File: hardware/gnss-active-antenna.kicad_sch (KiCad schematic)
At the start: 17 parts, among them J1 CONMCX002-SMD, U1 MAX2659ELT+T, U2 MIC5205-2.5YM5

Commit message: main: hardware: schematic update
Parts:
- C1: value 470pF -> 24pF
- C2: value 100 pF -> 24 pF
- C4: value 470 pF -> 33 nF
- C5: value 2.2 uF -> 10 uF
- C6: value 33 pF -> 33 nF
- L1: value 6.8 nH -> 6.2 nH
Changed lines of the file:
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@@
 			)
 		)
-		(property "Value" "6.8 nH"
+		(property "Value" "6.2 nH"
 			(at 99.06 48.26 90)
 			(effects
@@
 			)
 		)
-		(property "Value" "33 pF"
+		(property "Value" "33 nF"
 			(at 190.5 71.1199 0)
 			(effects
@@
 		(on_board yes)
 		(dnp no)
-		(fields_autoplaced yes)
 		(property "Reference" "C4"
-			(at 101.6 144.7799 0)
-			(effects
-				(font
-					(size 1.27 1.27)
-				)
-				(justify left)
-			)
-		)
-		(property "Value" "470 pF"
-			(at 101.6 147.3199 0)
-			(effects
-				(font
-					(size 1.27 1.27)
-				)
-				(justify left)
+			(at 101.854 148.844 0)
+			(effects
+				(font
+					(size 1.27 1.27)
+				)
+				(justify right)
+			)
+		)
+		(property "Value" "33 nF"
+			(at 107.442 149.352 0)
+			(effects
+				(font
+					(size 1.27 1.27)
+				)
+				(justify right)
 			)
 		)
@@
 			)
 		)
-		(property "Value" "100 pF"
+		(property "Value" "24 pF"
 			(at 229.87 49.53 90)
 			(effects
@@
 		(dnp no)
 		(property "Reference" "C5"
-			(at 113.03 144.7799 0)
+			(at 116.078 142.494 0)
 			(effects
 				(font
@@
 			)
 		)
-		(property "Value" "2.2 uF"
-			(at 113.03 147.3199 0)
+		(property "Value" "10 uF"
+			(at 125.222 143.51 0)
 			(effects
 				(font
@@
 			)
 		)
-		(property "Value" "470pF"
+		(property "Value" "24pF"
 			(at 86.36 45.72 90)
 			(effects

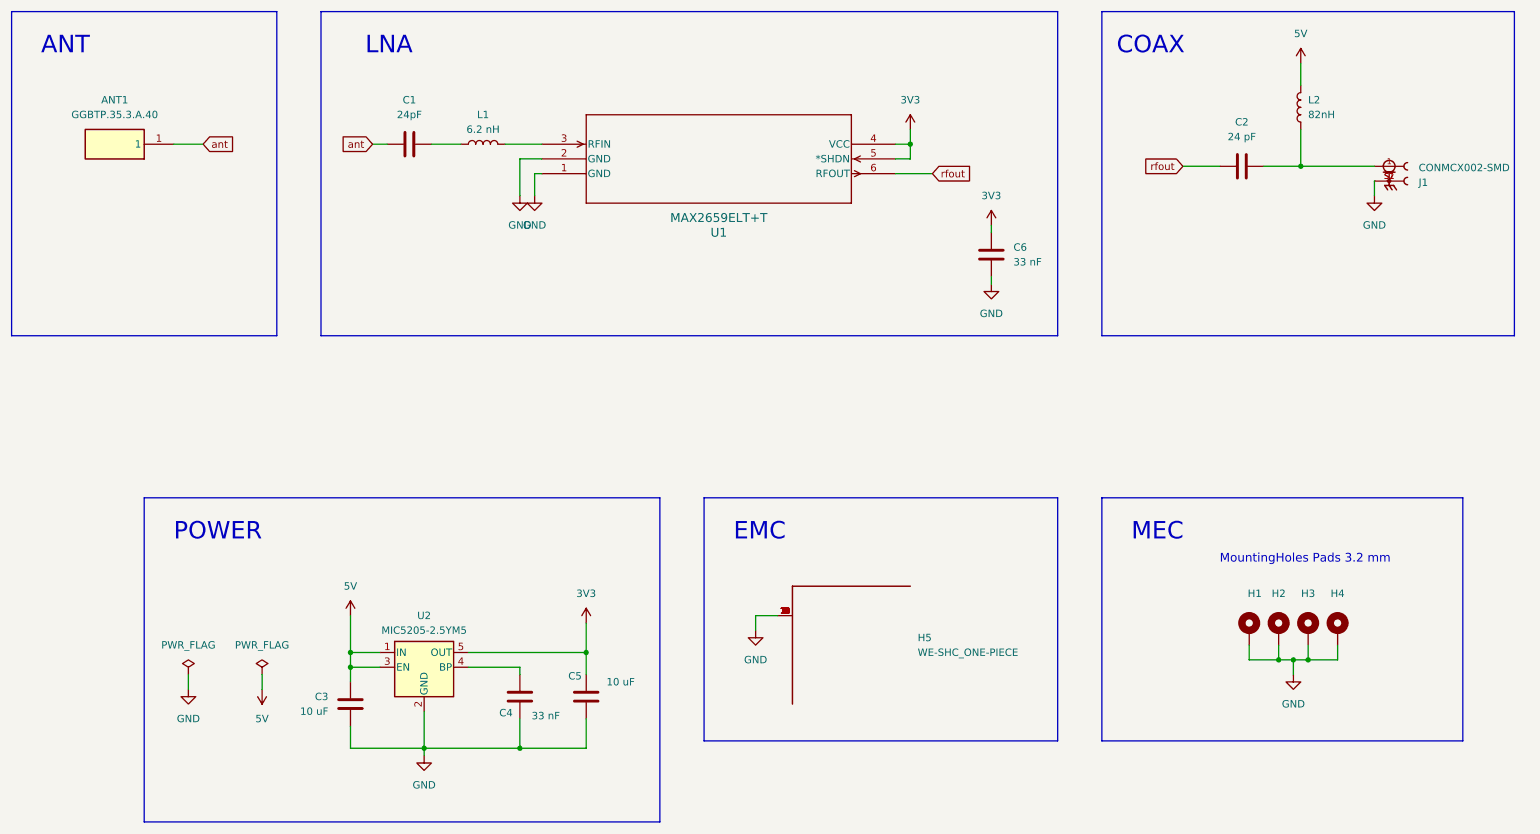
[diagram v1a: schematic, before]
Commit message: main: hardware: The bias-tee design was removed to make the first design simpler
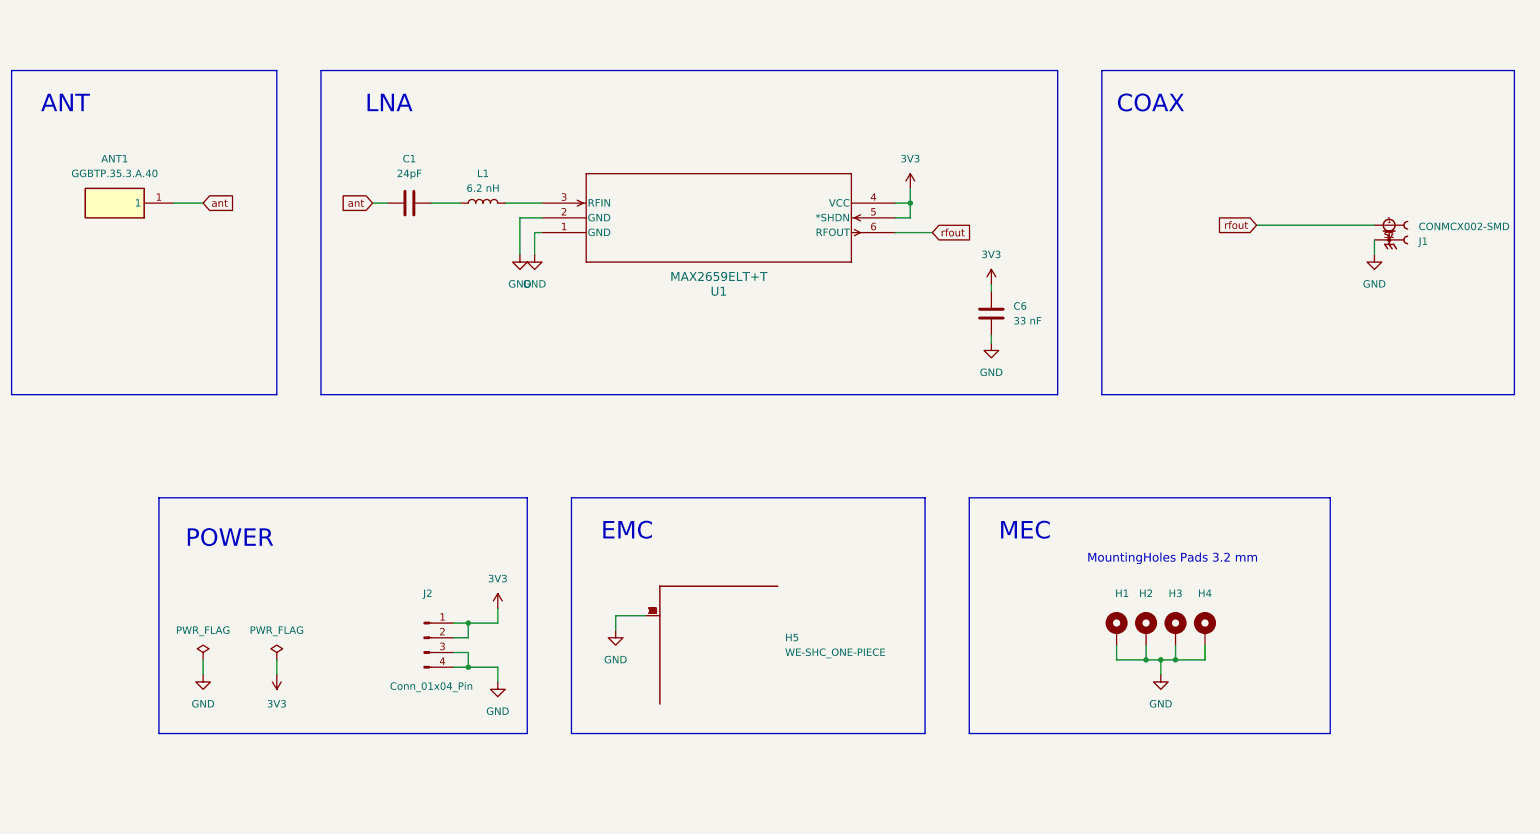
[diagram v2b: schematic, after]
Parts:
- removed C2: 24 pF, Capacitor_SMD:C_0402_1005Metric_Pad0.74x0.62mm_HandSolder, symbol Device:C
- removed C3, C5: 10 uF, Capacitor_SMD:C_0402_1005Metric_Pad0.74x0.62mm_HandSolder, symbol Device:C
- removed C4: 33 nF, Capacitor_SMD:C_0402_1005Metric_Pad0.74x0.62mm_HandSolder, symbol Device:C
- removed L2: 82nH, Capacitor_SMD:C_0402_1005Metric_Pad0.74x0.62mm_HandSolder, symbol Device:L
- removed U2: MIC5205-2.5YM5, Package_TO_SOT_SMD:SOT-23-5, symbol Regulator_Linear:MIC5205-2.5YM5
- added J2: Conn_01x04_Pin, Connector_Molex:Molex_PicoBlade_53261-0471_1x04-1MP_P1.25mm_Horizontal, symbol Connector:Conn_01x04_Pin
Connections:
- net 3V3: now also J2.1 (Pin_1), J2.2 (Pin_2)
- net GND: now also J2.3 (Pin_3), J2.4 (Pin_4)
- net rfout: now also J1.1
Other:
- moved on the sheet: ANT1, C1, C6, H1, H2, H3, H4, H5, J1, L1, U1
